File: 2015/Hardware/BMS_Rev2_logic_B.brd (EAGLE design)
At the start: 45.4 x 54 mm, 35 parts, among them Q9 MOSFET-NCHANNEL2N7002PW

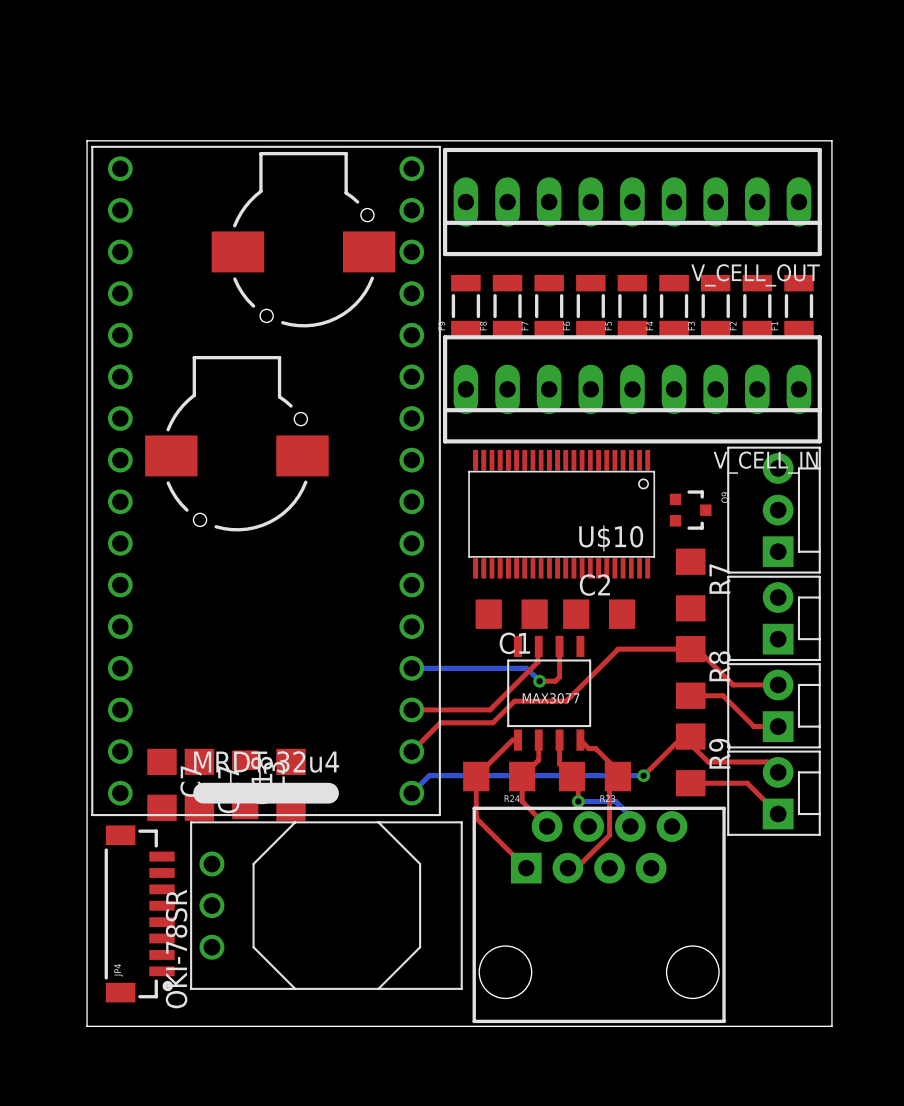
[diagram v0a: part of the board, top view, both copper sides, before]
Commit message: Pinswapped on the schematic side to make traces easier.
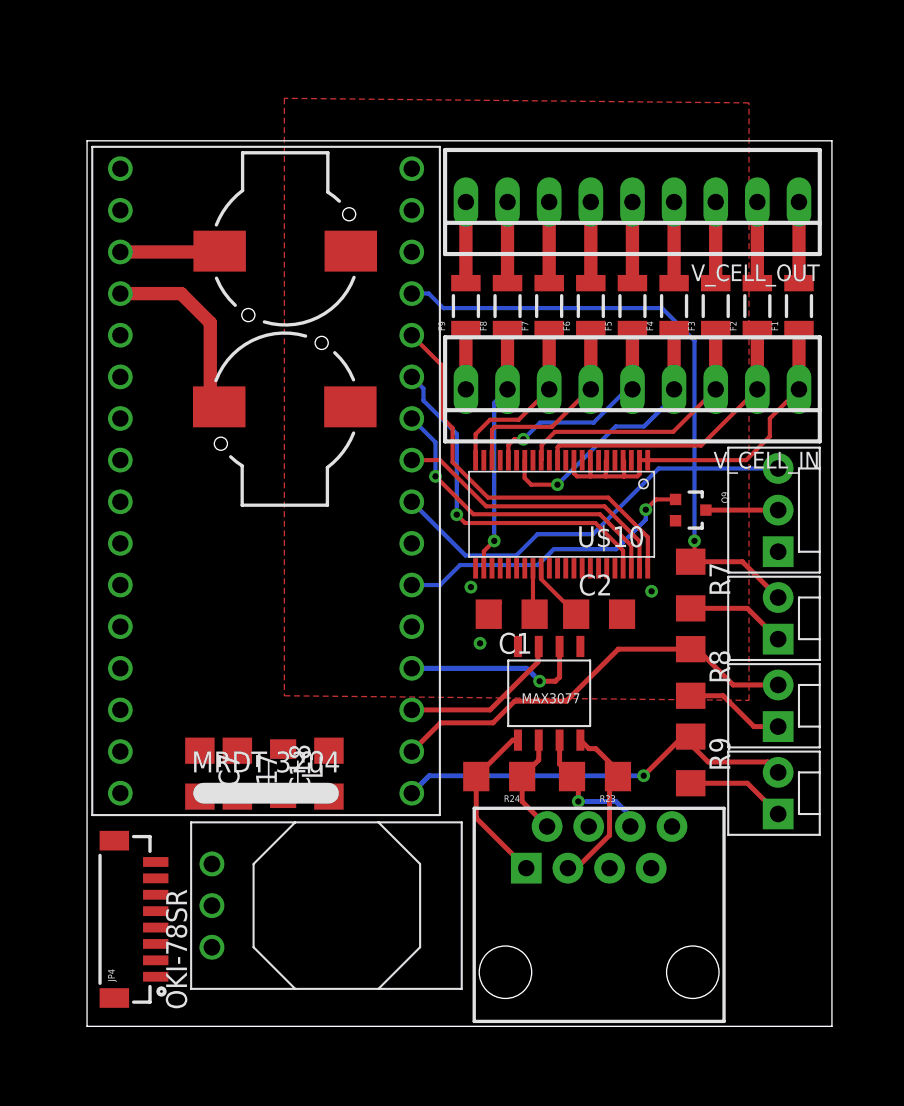
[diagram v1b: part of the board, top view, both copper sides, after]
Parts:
- moved BUZZER_1 4.19 mm to (12.1, 37.8), turned to 0 degrees
- moved C18 2.41 mm to (14.8, 15.4)
- moved L3 2.41 mm to (12.0, 15.4)
- moved C17 2.41 mm to (9.17, 15.4)
- moved C7 2.41 mm to (6.88, 15.4)
- moved BUZZER_2 1.12 mm to (12.1, 47.3)
- moved JP4 0.50 mm to (4.19, 6.53)
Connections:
- removed net N$63: U$3.19
- removed net N$64: U$3.20
- removed net SCL: U$3.6
- net BUZZ_1: now also U$3.20; no longer U$3.29
- net BUZZ_2: now also U$3.19; no longer U$3.28
- net LCD_ON: now also U$3.6; no longer U$3.26
- net LCD_TX: now also LCD.3
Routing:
- net SW_INSTALLED: track 0.00 -> 38.3 mm, vias 0 -> 1
- net LCD_TX: track 0.00 -> 25.9 mm
- net N$41: track 0.00 -> 24.6 mm
- net SS: track 0.00 -> 24.5 mm
- net SCK: track 0.00 -> 21.7 mm, vias 0 -> 1
- net MOSI: track 0.00 -> 19.2 mm, vias 0 -> 1
- net LCD_ON: track 0.00 -> 18.6 mm, vias 0 -> 1
- net N$42: track 0.00 -> 18.1 mm
- net MISO: track 0.00 -> 17.6 mm
- net N$89: track 0.00 -> 16.7 mm, vias 0 -> 1
- net N$43: track 0.00 -> 16.6 mm
- net N$48: track 0.00 -> 15.2 mm, vias 0 -> 1
- net N$91: track 0.00 -> 13.6 mm, vias 0 -> 1
- net N$46: track 0.00 -> 12.6 mm
- net BUZZ_1: track 0.00 -> 11.6 mm
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- added copper zone on layer 1, net GND

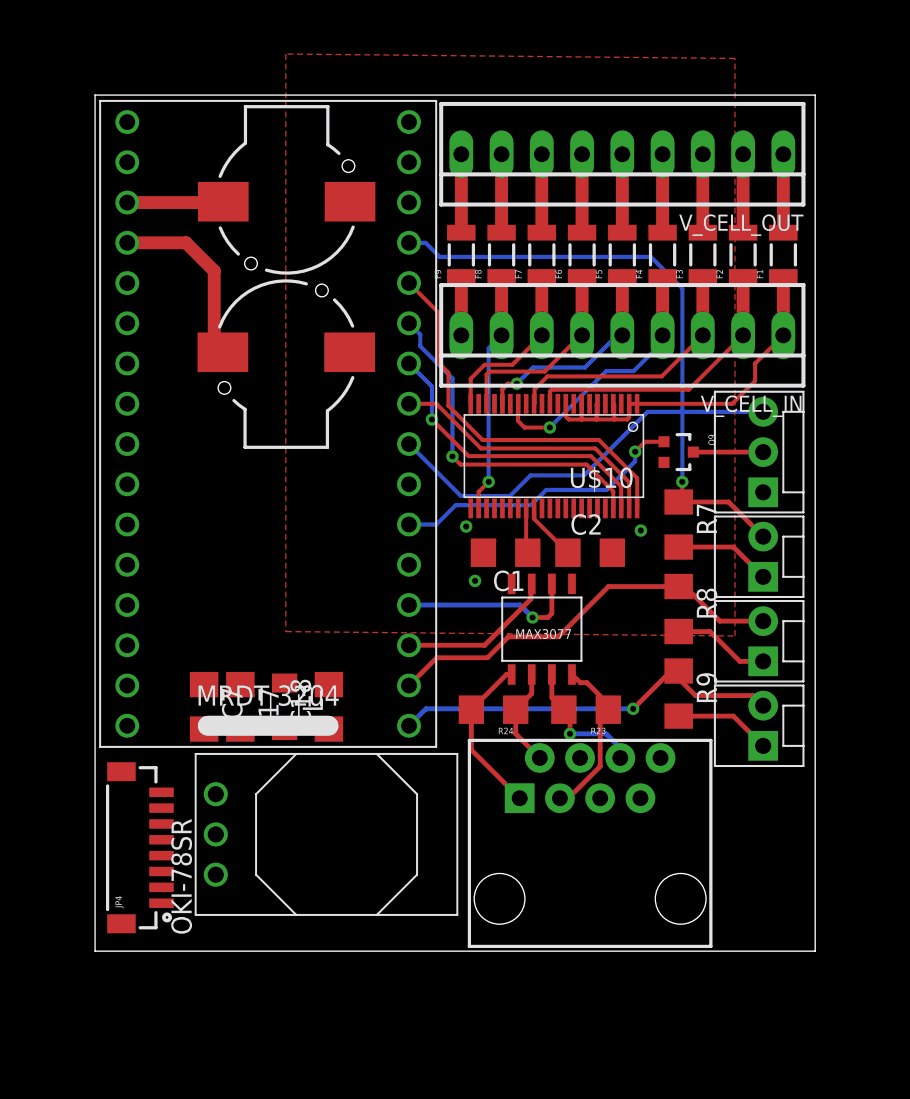
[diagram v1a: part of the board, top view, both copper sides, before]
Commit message: Added Mounting Holes
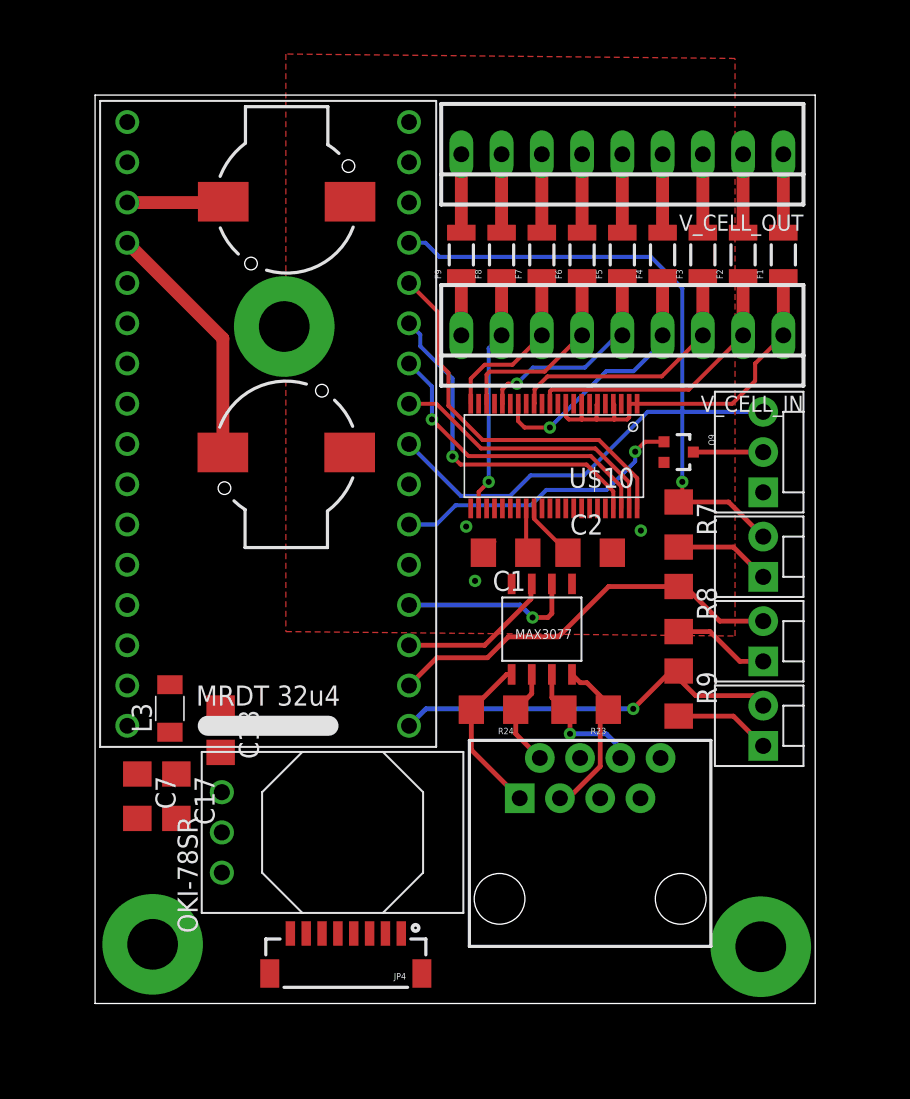
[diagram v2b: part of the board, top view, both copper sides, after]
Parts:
- added S1, S2, S3: STANDOFF_ELECTRICAL, SparkFun-Electromechanical:STANDOFF-ELECTRICAL
- moved JP4 12.8 mm to (15.8, 1.12), turned to 180 degrees
- moved L3 7.24 mm to (4.72, 15.3), turned to 90 degrees
- moved C7 7.04 mm to (2.67, 9.78)
- moved C18 6.99 mm to (7.92, 13.9), turned to 270 degrees
- moved C17 6.94 mm to (5.13, 9.78)
- moved BUZZER_1 6.32 mm to (12.1, 31.5)
- moved OKI-78SR 0.40 mm to (8.00, 7.49)
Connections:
- net GND: now also S1.P1, S2.P1, S3.P1
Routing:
- net BUZZ_1: track 11.6 -> 15.7 mm
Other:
- board size 45.4 x 54 mm -> 45.4 x 57.3 mm
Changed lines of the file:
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@@
 <board>
 <plain>
-<wire x1="0" y1="0" x2="45.446" y2="0" width="0" layer="20"/>
-<wire x1="45.446" y1="0" x2="45.446" y2="54.026" width="0" layer="20"/>
+<wire x1="0" y1="-3.302" x2="45.446" y2="-3.302" width="0" layer="20"/>
+<wire x1="45.446" y1="-3.302" x2="45.446" y2="54.026" width="0" layer="20"/>
 <wire x1="45.446" y1="54.026" x2="0" y2="54.026" width="0" layer="20"/>
-<wire x1="0" y1="54.026" x2="0" y2="0" width="0" layer="20"/>
+<wire x1="0" y1="54.026" x2="0" y2="-3.302" width="0" layer="20"/>
 <dimension x1="0" y1="54.026" x2="45.446" y2="54.026" x3="22.723" y3="59.182" textsize="1.778" layer="21" unit="inch"/>
 <dimension x1="45.446" y1="54.026" x2="45.446" y2="0" x3="66.04" y3="27.013" textsize="1.778" layer="21" unit="inch"/>
@@
 <elements>
 <element name="U$3" library="MRDT-2015-General" package="32U4_MCU_DIP" value="32U4_BREAKOUT" x="10.922" y="33.274" rot="R180"/>
-<element name="OKI-78SR" library="MRDT-2015-PowerBoard" package="OKI-78SRH" value="Q_OKI-78SR" x="7.62" y="7.366" rot="R270"/>
-<element name="C17" library="resistor" package="C1206" value="47µF" x="9.1694" y="15.4178" rot="R270"/>
-<element name="L3" library="resistor" package="L3216C" value="" x="11.9634" y="15.4178" rot="R270"/>
-<element name="C18" library="resistor" package="C1206" value="47µF" x="14.7574" y="15.4178" rot="R90"/>
+<element name="OKI-78SR" library="MRDT-2015-PowerBoard" package="OKI-78SRH" value="Q_OKI-78SR" x="8.001" y="7.493" rot="R270"/>
+<element name="C17" library="resistor" package="C1206" value="47µF" x="5.1308" y="9.779" rot="R270"/>
+<element name="L3" library="resistor" package="L3216C" value="" x="4.7244" y="15.3162" rot="R90"/>
+<element name="C18" library="resistor" package="C1206" value="47µF" x="7.9248" y="13.9446" rot="R270"/>
 <element name="U$6" library="SparkFun-Connectors" package="RJ45-8" value="RJ45-8PTH" x="31.242" y="3.302"/>
 <element name="R23" library="SparkFun-Passives" package="1206" value="120 Ohm" x="30.988" y="15.24" rot="R180"/>
 <element name="R24" library="SparkFun-Passives" package="1206" value="120 Ohm" x="25.146" y="15.24" rot="R180"/>
-<element name="C7" library="resistor" package="C1206" value="1uF" x="6.8834" y="15.4178" rot="R270"/>
+<element name="C7" library="resistor" package="C1206" value="1uF" x="2.667" y="9.779" rot="R270"/>
 <element name="U$9" library="MAX3077" package="MAX3070E" value="MAX3077" x="28.194" y="20.32" rot="R180"/>
 <element name="V_CELL_IN" library="con-molex" package="22-23-2091" value="22-23-2091" x="33.274" y="38.862" rot="R180">
@@
 <element name="R9" library="resistor" package="R1206" value="10kΩ" x="36.83" y="16.256" rot="R270"/>
 <element name="BUZZER_2" library="SparkFun-Electromechanical" package="BUZZER-CCV" value="BUZZERSMD2" x="12.0904" y="47.2948" rot="R180"/>
-<element name="BUZZER_1" library="SparkFun-Electromechanical" package="BUZZER-CCV" value="BUZZERSMD2" x="12.065" y="37.7952"/>
+<element name="BUZZER_1" library="SparkFun-Electromechanical" package="BUZZER-CCV" value="BUZZERSMD2" x="12.065" y="31.4706"/>
 <element name="U$10" library="MRDT-2015-BMS" package="SSOP44" value="Q_LTC6802-2" x="28.956" y="31.242" rot="R180"/>
 <element name="C1" library="resistor" package="C1206" value="1µF" x="25.908" y="25.146" rot="R180"/>
@@
 <attribute name="PROD_ID" value="RES-11150" x="106.934" y="64.262" size="1.778" layer="27" rot="R90" display="off"/>
 </element>
-<element name="JP4" library="SparkFun-Connectors" package="BM08B-SRSS-TB" value="" x="4.191" y="6.5278" rot="R90"/>
+<element name="JP4" library="SparkFun-Connectors" package="BM08B-SRSS-TB" value="" x="15.8242" y="1.1176" rot="R180"/>
 <element name="F9" library="SparkFun-PowerIC" package="PTC-1206" value="PTCSMD" x="23.114" y="43.942" rot="R90">
 <attribute name="PROD_ID" value="RES-11150" x="104.394" y="69.342" size="1.778" layer="27" rot="R90" display="off"/>
 </element>
 <element name="LCD" library="SparkFun-Connectors" package="MOLEX-1X3" value="" x="42.164" y="28.956" rot="R90"/>
+<element name="S1" library="SparkFun-Electromechanical" package="STANDOFF-ELECTRICAL" value="STANDOFF_ELECTRICAL" x="42.0116" y="0.2794"/>
+<element name="S2" library="SparkFun-Electromechanical" package="STANDOFF-ELECTRICAL" value="STANDOFF_ELECTRICAL" x="3.6322" y="0.4318"/>
+<element name="S3" library="SparkFun-Electromechanical" package="STANDOFF-ELECTRICAL" value="STANDOFF_ELECTRICAL" x="11.938" y="39.4208"/>
 </elements>
 <signals>
@@
 <vertex x="40.386" y="56.3372"/>
 </polygon>
-<wire x1="19.812" y1="49.784" x2="16.0904" y2="47.2948" width="0" layer="19" extent="1-1"/>
-<wire x1="25.206" y1="27.942" x2="25.206" y2="25.844" width="0" layer="19" extent="1-1"/>
-<wire x1="4.191" y1="10.0278" x2="7.62" y2="7.366" width="0" layer="19" extent="1-1"/>
-<wire x1="6.8834" y1="14.0178" x2="4.191" y2="10.0278" width="0" layer="19" extent="1-1"/>
-<wire x1="9.1694" y1="14.0178" x2="6.8834" y2="14.0178" width="0" layer="19" extent="1-1"/>
-<wire x1="14.7574" y1="16.8178" x2="9.1694" y2="14.0178" width="0" layer="19" extent="1-1"/>
-<wire x1="16.065" y1="37.7952" x2="16.0904" y2="47.2948" width="0" layer="19" extent="1-1"/>
+<contactref element="S1" pad="P1"/>
+<contactref element="S2" pad="P1"/>
+<contactref element="S3" pad="P1"/>
+<wire x1="25.206" y1="25.844" x2="25.206" y2="27.942" width="0" layer="19" extent="1-1"/>
+<wire x1="5.1308" y1="8.379" x2="8.001" y2="7.493" width="0" layer="19" extent="1-1"/>
+<wire x1="2.667" y1="8.379" x2="5.1308" y2="8.379" width="0" layer="19" extent="1-1"/>
+<wire x1="7.9248" y1="12.5446" x2="5.1308" y2="8.379" width="0" layer="19" extent="1-1"/>
+<wire x1="12.3242" y1="1.1176" x2="8.001" y2="7.493" width="0" layer="19" extent="1-1"/>
 </signal>
 <signal name="GATE">
 <contactref element="U$3" pad="25"/>
 <contactref element="JP4" pad="6"/>
-<wire x1="4.191" y1="8.0278" x2="2.032" y2="32.004" width="0" layer="19" extent="1-1"/>
+<wire x1="14.3242" y1="1.1176" x2="2.032" y2="32.004" width="0" layer="19" extent="1-1"/>
 </signal>
 <signal name="I_ARRAY">
 <contactref element="U$3" pad="24"/>
 <contactref element="JP4" pad="2"/>
-<wire x1="4.191" y1="4.0278" x2="2.032" y2="34.544" width="0" layer="19" extent="1-1"/>
+<wire x1="18.3242" y1="1.1176" x2="2.032" y2="34.544" width="0" layer="19" extent="1-1"/>
 </signal>
 <signal name="SDA">
@@
 <contactref element="L3" pad="1"/>
 <contactref element="OKI-78SR" pad="3"/>
-<wire x1="9.1694" y1="16.8178" x2="11.9634" y2="16.9178" width="0" layer="19" extent="1-1"/>
-<wire x1="7.62" y1="9.906" x2="9.1694" y2="16.8178" width="0" layer="19" extent="1-1"/>
+<wire x1="4.7244" y1="13.8162" x2="5.1308" y2="11.179" width="0" layer="19" extent="1-1"/>
+<wire x1="8.001" y1="10.033" x2="5.1308" y2="11.179" width="0" layer="19" extent="1-1"/>
 </signal>
 <signal name="RXD">
@@
 <contactref element="BUZZER_1" pad="-"/>
 <contactref element="U$3" pad="20"/>
-<wire x1="2.032" y1="44.704" x2="5.7404" y2="44.704" width="0.8128" layer="1"/>
-<wire x1="5.7404" y1="44.704" x2="7.5184" y2="42.926" width="0.8128" layer="1"/>
-<wire x1="7.5184" y1="42.926" x2="7.5184" y2="38.3418" width="0.8128" layer="1"/>
-<wire x1="7.5184" y1="38.3418" x2="8.065" y2="37.7952" width="0.8128" layer="1"/>
+<wire x1="2.032" y1="44.704" x2="8.065" y2="38.671" width="0.8128" layer="1"/>
+<wire x1="8.065" y1="38.671" x2="8.065" y2="31.4706" width="0.8128" layer="1"/>
 </signal>
 <signal name="BUZZ_2">
@@
 <contactref element="JP4" pad="7"/>
 <contactref element="U$3" pad="23"/>
-<wire x1="4.191" y1="9.0278" x2="2.032" y2="37.084" width="0" layer="19" extent="1-1"/>
+<wire x1="13.3242" y1="1.1176" x2="2.032" y2="37.084" width="0" layer="19" extent="1-1"/>
 </signal>
 <signal name="V_CHECK">
 <contactref element="JP4" pad="4"/>
 <contactref element="U$3" pad="21"/>
-<wire x1="4.191" y1="6.0278" x2="2.032" y2="42.164" width="0" layer="19" extent="1-1"/>
+<wire x1="16.3242" y1="1.1176" x2="2.032" y2="42.164" width="0" layer="19" extent="1-1"/>
 </signal>
 <signal name="V_CHG">
 <contactref element="JP4" pad="1"/>
 <contactref element="U$3" pad="22"/>
-<wire x1="4.191" y1="3.0278" x2="2.032" y2="39.624" width="0" layer="19" extent="1-1"/>
+<wire x1="19.3242" y1="1.1176" x2="2.032" y2="39.624" width="0" layer="19" extent="1-1"/>
 </signal>
 <signal name="LOGIC_POWER">
 <contactref element="JP4" pad="3"/>
 <contactref element="OKI-78SR" pad="1"/>
-<wire x1="4.191" y1="5.0278" x2="7.62" y2="4.826" width="0" layer="19" extent="1-1"/>
+<wire x1="8.001" y1="4.953" x2="17.3242" y2="1.1176" width="0" layer="19" extent="1-1"/>
 </signal>
 <signal name="N$4">
